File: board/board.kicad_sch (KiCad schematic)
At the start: 1 part

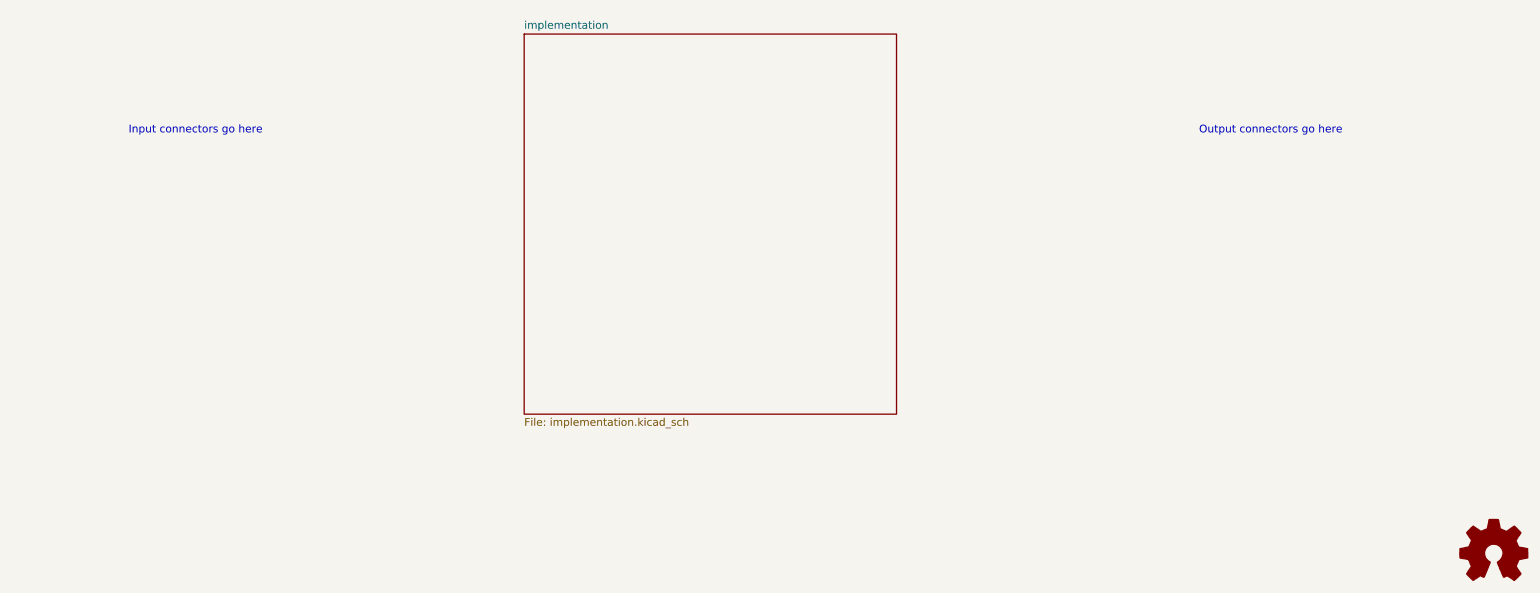
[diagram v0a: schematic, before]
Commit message: added schematic and footprint from legacy project
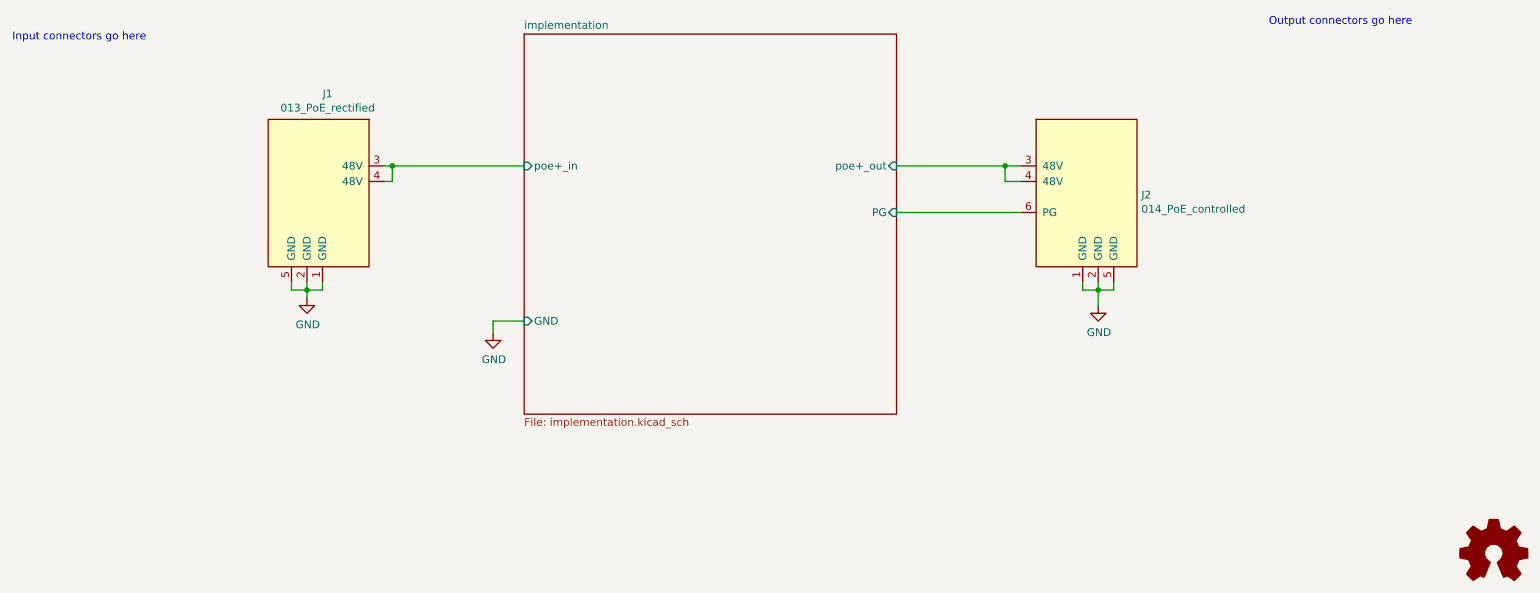
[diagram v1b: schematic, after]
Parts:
- added J1: 013_PoE_rectified, on_edge:on_edge_2x05_device, symbol put_on_edge:013_PoE_rectified
- added J2: 014_PoE_controlled, on_edge:on_edge_2x05_host, symbol put_on_edge:014_PoE_controlled
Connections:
- new net GND: J1.1 (GND), J1.2 (GND), J1.5 (GND), J2.1 (GND), J2.2 (GND), J2.5 (GND)
- new net implementation/PG: J2.6 (PG)
- new net implementation/poe+_in: J1.3 (48V), J1.4 (48V)
- new net implementation/poe+_out: J2.3 (48V), J2.4 (48V)
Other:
- sheet implementation ports: added GND, PG, poe+_in, poe+_out; removed none
